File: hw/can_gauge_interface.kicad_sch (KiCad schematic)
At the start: 58 parts, among them J1 USB_B, J10 +5VA, J2 Conn_02x04_Top_Bottom, J3 Analog, J4 ICSP, J5 SPI Debug, J6 CAN ~{CS}, J7 ROM ~{CS}, J8 DAC ~{CS}, J9 Conn_01x04_Socket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

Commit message: routing
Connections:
- net DAC1_~{CS}: now also U1.12 (RB5/AN11/RX/DX)
- net DAC2_~{CS}: now also U1.10 (RB7/TX/CK)
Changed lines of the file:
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@@
+	(wire
+		(pts
+			(xy 298.45 80.01) (xy 308.61 80.01)
+		)
+		(stroke
+			(width 0)
+			(type default)
+		)
+	)
 	(wire
 		(pts
@@
 		(pts
 			(xy 233.68 152.4) (xy 233.68 182.88)
+		)
+		(stroke
+			(width 0)
+			(type default)
+		)
+	)
+	(wire
+		(pts
+			(xy 298.45 85.09) (xy 308.61 85.09)
 		)
 		(stroke
@@
 	)
 	(label "DAC1_~{CS}"
-		(at 318.77 46.99 0)
+		(at 298.45 80.01 0)
 		(effects
 			(font
@@
 	)
 	(label "DAC2_~{CS}"
-		(at 317.5 43.18 0)
-		(effects
-			(font
+		(at 298.45 85.09 0)
+		(effects
+			(font

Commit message: more routing
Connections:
- net DAC1_~{CS}: now also J8.2 (Pin_2), U1.10 (RB7/TX/CK); no longer J8.1 (Pin_1), U1.12 (RB5/AN11/RX/DX)
- net DAC2_~{CS}: now also J8.1 (Pin_1), U1.12 (RB5/AN11/RX/DX); no longer J8.2 (Pin_2), U1.10 (RB7/TX/CK)
- net Speed: now also U1.6 (CWG1B/C1OUT/C2OUT/RC4)
- net Tach: now also U1.7 (CLKR/C1IN3-/C2IN3-/DACOUT2/AN7/RC3)
- no-connect marks 7 -> 9
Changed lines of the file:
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@@
 	)
 	(no_connect
+		(at 410.21 67.31)
+	)
+	(no_connect
 		(at 200.66 185.42)
 	)
@@
 	)
 	(no_connect
+		(at 410.21 77.47)
+	)
+	(no_connect
 		(at 231.14 180.34)
 	)
@@
 	(wire
 		(pts
+			(xy 410.21 72.39) (xy 424.18 72.39)
+		)
+		(stroke
+			(width 0)
+			(type default)
+		)
+	)
+	(wire
+		(pts
 			(xy 391.16 134.62) (xy 391.16 139.7)
 		)
@@
 	(wire
 		(pts
+			(xy 410.21 69.85) (xy 424.18 69.85)
+		)
+		(stroke
+			(width 0)
+			(type default)
+		)
+	)
+	(wire
+		(pts
 			(xy 261.62 176.53) (xy 261.62 170.18)
 		)
@@
 	)
 	(label "DAC1_~{CS}"
-		(at 298.45 80.01 0)
+		(at 298.45 85.09 0)
 		(effects
 			(font
@@
 	)
 	(label "DAC2_~{CS}"
-		(at 298.45 85.09 0)
+		(at 298.45 80.01 0)
 		(effects
 			(font
@@
 	)
 	(label "DAC1_~{CS}"
-		(at 57.15 313.69 180)
+		(at 57.15 316.23 180)
 		(effects
 			(font
@@
 	)
 	(label "DAC2_~{CS}"
-		(at 57.15 316.23 180)
+		(at 57.15 313.69 180)
 		(effects
 			(font

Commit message: drc
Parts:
- J1: footprint Connector_USB:USB_B_Lumberg_2411_02_Horizontal -> footprints:USB_B_Lumberg_2411_02_Horizontal
- J2: footprint Connector_Molex:Molex_Mini-Fit_Jr_5569-08A2_2x04_P4.20mm_Horizontal -> footprints:Molex_Mini-Fit_Jr_5569-08A2_2x04_P4.20mm_Horizontal
- J3: footprint Connector_Molex:Molex_Mini-Fit_Jr_5569-06A2_2x03_P4.20mm_Horizontal -> footprints:Molex_Mini-Fit_Jr_5569-06A2_2x03_P4.20mm_Horizontal
- U5: footprint Package_SO:TI_SO-PowerPAD-8_ThermalVias -> Package_SO:TI_SO-PowerPAD-8
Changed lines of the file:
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@@
 			)
 		)
-		(property "Footprint" "Package_SO:TI_SO-PowerPAD-8_ThermalVias"
+		(property "Footprint" "Package_SO:TI_SO-PowerPAD-8"
 			(at 64.77 64.77 0)
 			(effects
@@
 			)
 		)
-		(property "Footprint" "Connector_Molex:Molex_Mini-Fit_Jr_5569-08A2_2x04_P4.20mm_Horizontal"
+		(property "Footprint" "footprints:Molex_Mini-Fit_Jr_5569-08A2_2x04_P4.20mm_Horizontal"
 			(at 49.53 233.68 0)
 			(effects
@@
 			)
 		)
-		(property "Footprint" "Connector_USB:USB_B_Lumberg_2411_02_Horizontal"
+		(property "Footprint" "footprints:USB_B_Lumberg_2411_02_Horizontal"
 			(at 44.45 205.74 0)
 			(effects
@@
 			)
 		)
-		(property "Footprint" "Connector_Molex:Molex_Mini-Fit_Jr_5569-06A2_2x03_P4.20mm_Horizontal"
+		(property "Footprint" "footprints:Molex_Mini-Fit_Jr_5569-06A2_2x03_P4.20mm_Horizontal"
 			(at 49.53 260.35 0)
 			(effects

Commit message: tune usb trace length
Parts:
- C10, C12, C13, C14, C15, C16, C17, J4, R10, R11, R6, R7, R9, U1, U2, U3, U4, U8, U9: now not fitted
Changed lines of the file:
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@@
 		(in_bom yes)
 		(on_board yes)
-		(dnp no)
+		(dnp yes)
 		(property "Reference" "C15"
 			(at 383.54 133.35 90)
@@
 		(in_bom yes)
 		(on_board yes)
-		(dnp no)
+		(dnp yes)
 		(property "Reference" "C14"
 			(at 266.7 143.51 90)
@@
 		(in_bom yes)
 		(on_board yes)
-		(dnp no)
+		(dnp yes)
 		(property "Reference" "U4"
 			(at 395.605 148.59 0)
@@
 		(in_bom yes)
 		(on_board yes)
-		(dnp no)
+		(dnp yes)
 		(property "Reference" "R7"
 			(at 200.025 152.4 0)
@@
 		(in_bom yes)
 		(on_board yes)
-		(dnp no)
+		(dnp yes)
 		(property "Reference" "R9"
 			(at 374.015 149.86 0)
@@
 		(in_bom yes)
 		(on_board yes)
-		(dnp no)
+		(dnp yes)
 		(property "Reference" "C13"
 			(at 201.93 135.89 90)
@@
 		(in_bom yes)
 		(on_board yes)
-		(dnp no)
+		(dnp yes)
 		(fields_autoplaced yes)
 		(property "Reference" "C12"
@@
 		(in_bom yes)
 		(on_board yes)
-		(dnp no)
+		(dnp yes)
 		(property "Reference" "C17"
 			(at 533.4 161.29 90)
@@
 		(in_bom yes)
 		(on_board yes)
-		(dnp no)
+		(dnp yes)
 		(property "Reference" "U8"
 			(at 528.955 111.76 0)
@@
 		(in_bom yes)
 		(on_board yes)
-		(dnp no)
+		(dnp yes)
 		(property "Reference" "U3"
 			(at 284.48 156.21 0)
@@
 		(in_bom yes)
 		(on_board yes)
-		(dnp no)
+		(dnp yes)
 		(property "Reference" "R6"
 			(at 274.955 58.42 0)
@@
 		(in_bom yes)
 		(on_board yes)
-		(dnp no)
+		(dnp yes)
 		(property "Reference" "C10"
 			(at 350.52 41.275 90)
@@
 		(in_bom yes)
 		(on_board yes)
-		(dnp no)
+		(dnp yes)
 		(property "Reference" "J4"
 			(at 36.195 168.275 0)
@@
 		(in_bom yes)
 		(on_board yes)
-		(dnp no)
+		(dnp yes)
 		(property "Reference" "U2"
 			(at 226.06 156.21 0)
@@
 		(in_bom yes)
 		(on_board yes)
-		(dnp no)
+		(dnp yes)
 		(property "Reference" "C16"
 			(at 533.4 97.79 90)
@@
 		(in_bom yes)
 		(on_board yes)
-		(dnp no)
+		(dnp yes)
 		(property "Reference" "U9"
 			(at 528.955 175.26 0)
@@
 		(in_bom yes)
 		(on_board yes)
-		(dnp no)
+		(dnp yes)
 		(property "Reference" "R10"
 			(at 502.285 111.76 0)
@@
 		(in_bom yes)
 		(on_board yes)
-		(dnp no)
+		(dnp yes)
 		(property "Reference" "U1"
 			(at 403.225 52.07 0)
@@
 		(in_bom yes)
 		(on_board yes)
-		(dnp no)
+		(dnp yes)
 		(property "Reference" "R11"
 			(at 502.285 175.26 0)

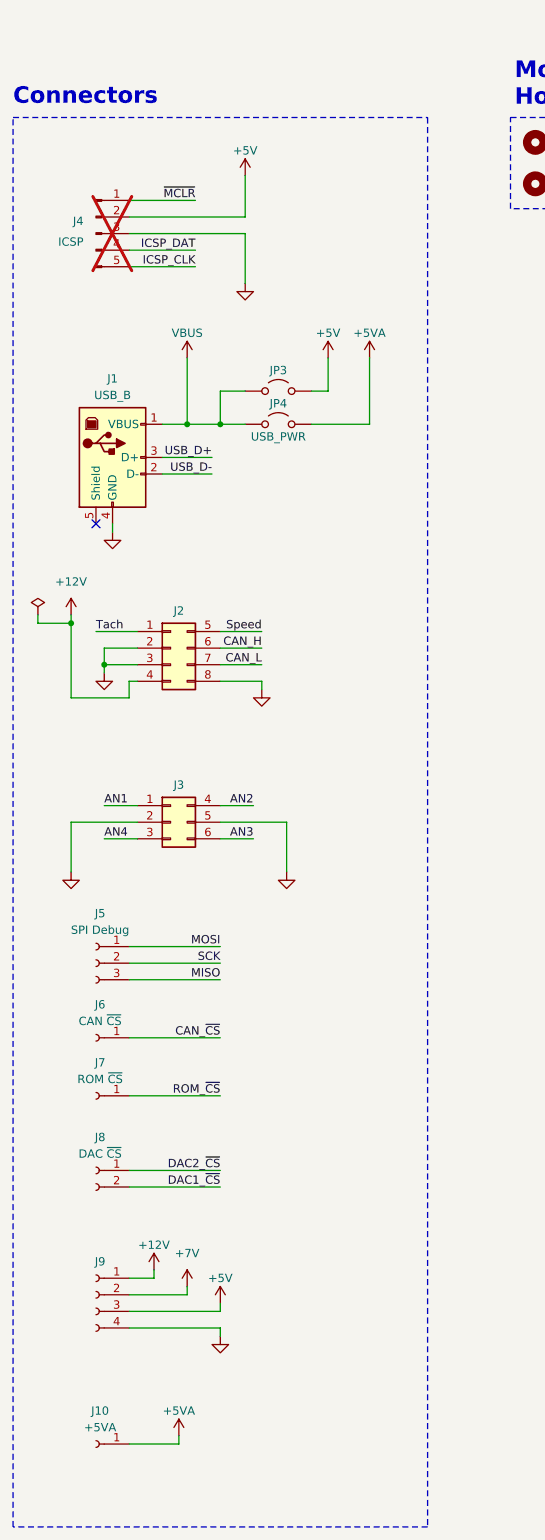
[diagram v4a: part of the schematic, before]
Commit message: removed usb vbus
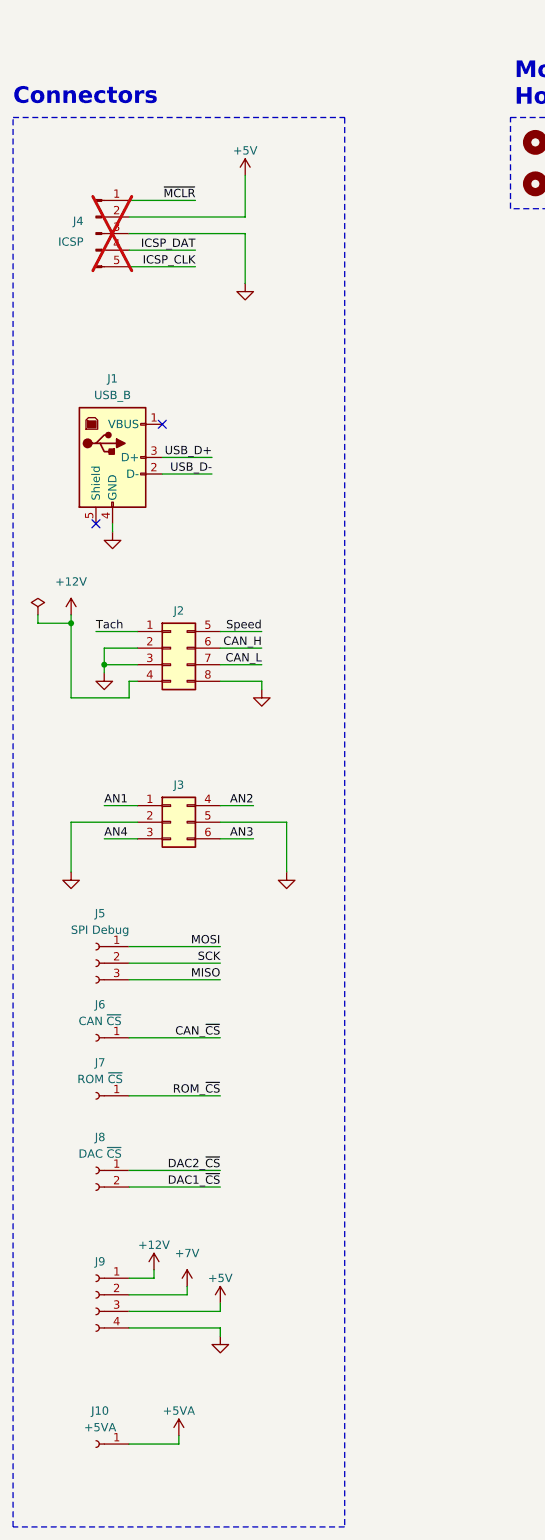
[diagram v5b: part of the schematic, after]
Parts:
- removed JP3, JP4: USB_PWR, Connector_PinSocket_2.54mm:PinSocket_1x02_P2.54mm_Vertical, symbol Jumper:Jumper_2_Open
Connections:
- net VBUS: no longer names the net of J1.1 (VBUS)
- no-connect marks 9 -> 10

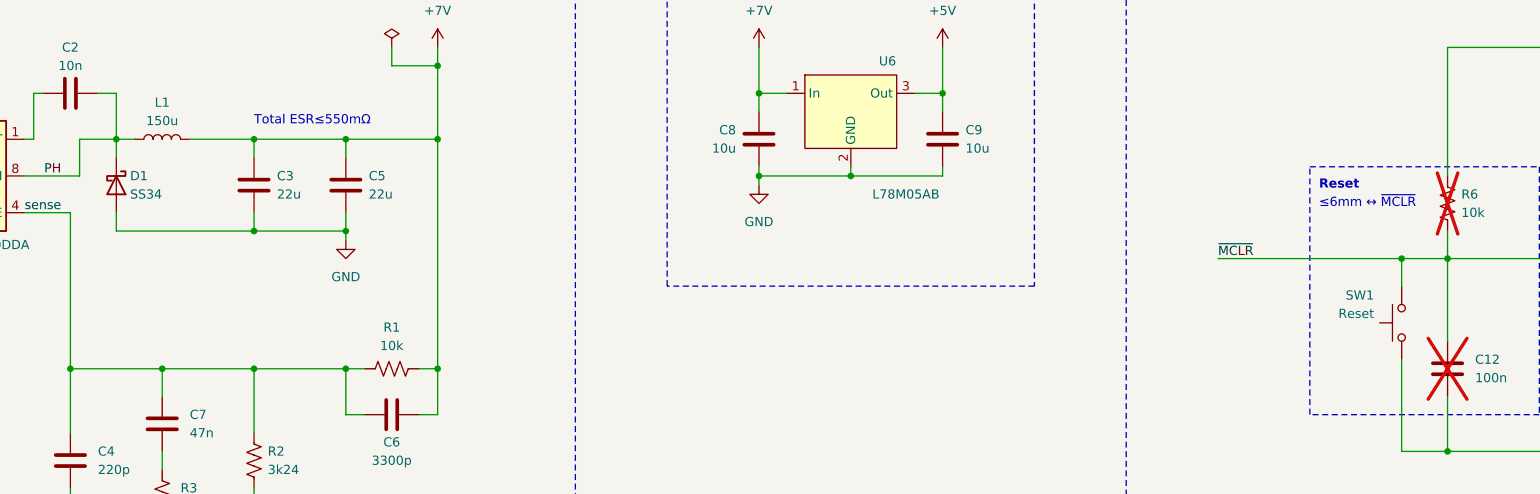
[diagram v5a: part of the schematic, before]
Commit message: gnd pours
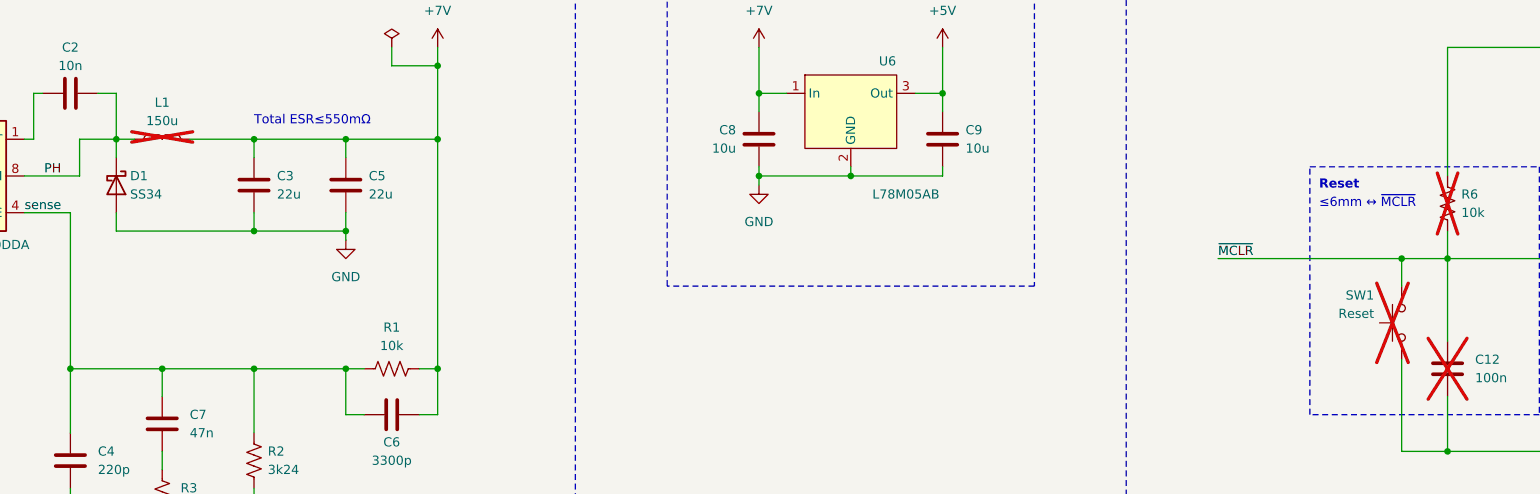
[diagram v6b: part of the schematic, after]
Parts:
- JP2: now in the parts list
- L1: footprint Inductor_SMD:L_12x12mm_H8mm -> Inductor_SMD:L_Wuerth_WE-PD-Typ-LS_Handsoldering; now not fitted
- SW1: now not fitted
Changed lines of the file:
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@@
 	(title_block
 		(title "CAN Gauge Interface")
-		(date "2025-09-19")
-		(rev "0.1")
+		(date "2025-10-01")
+		(rev "0.2")
 		(company "Sam Anthony")
 	)
@@
 		(unit 1)
 		(exclude_from_sim no)
-		(in_bom no)
+		(in_bom yes)
 		(on_board yes)
 		(dnp no)
@@
 		(in_bom yes)
 		(on_board yes)
-		(dnp no)
+		(dnp yes)
 		(fields_autoplaced yes)
 		(property "Reference" "L1"
@@
 			)
 		)
-		(property "Footprint" "Inductor_SMD:L_12x12mm_H8mm"
+		(property "Footprint" "Inductor_SMD:L_Wuerth_WE-PD-Typ-LS_Handsoldering"
 			(at 95.25 50.8 0)
 			(effects
@@
 			)
 		)
-		(property "Datasheet" "~"
+		(property "Datasheet" "https://www.we-online.com/components/products/datasheet/7447706151.pdf"
 			(at 95.25 50.8 0)
 			(effects
@@
 		(in_bom yes)
 		(on_board yes)
-		(dnp no)
+		(dnp yes)
 		(property "Reference" "SW1"
 			(at 262.89 72.39 90)

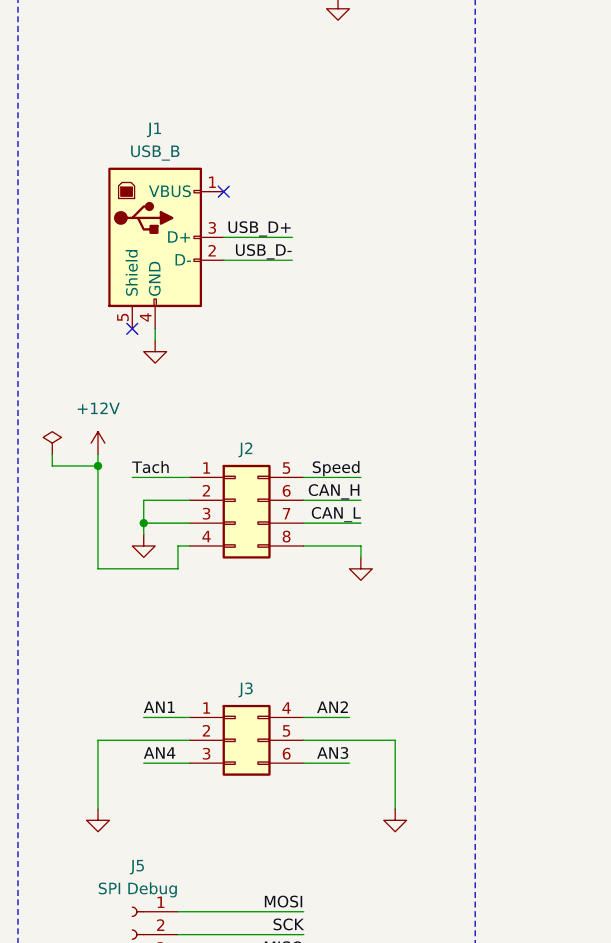
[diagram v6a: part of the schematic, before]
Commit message: connector 3d models
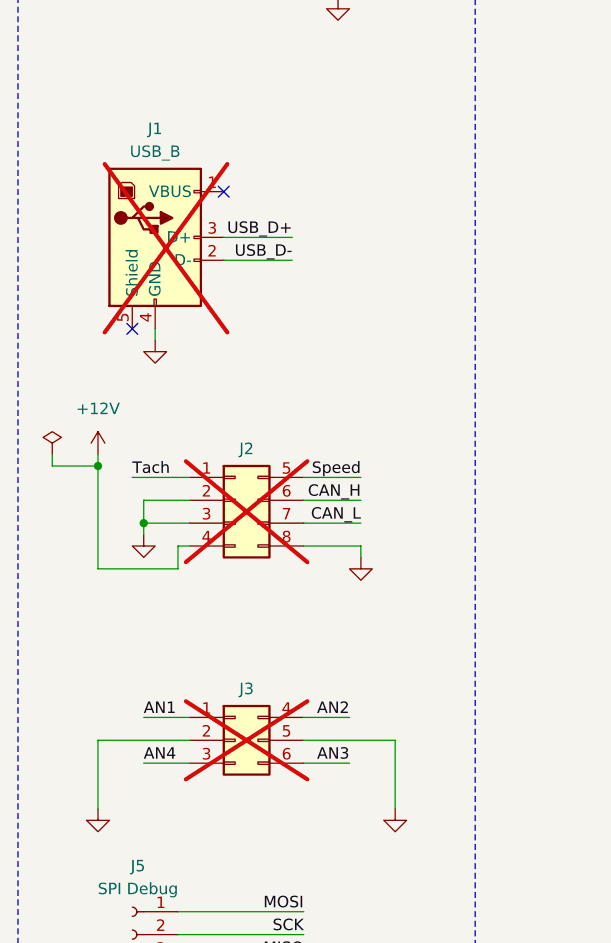
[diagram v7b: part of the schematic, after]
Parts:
- J1: footprint footprints:USB_B_Lumberg_2411_02_Horizontal -> USB_B_Samtec_USB-B-S-F-W-TH:SAMTEC_USB-B-S-X-X-TH; now not fitted
- J2, J3: now not fitted
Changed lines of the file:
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@@
 	)
 	(no_connect
-		(at 38.1 214.63)
-	)
-	(no_connect
 		(at 48.26 199.39)
 	)
@@
 		(at 231.14 180.34)
 	)
+	(no_connect
+		(at 38.1 214.63)
+	)
 	(wire
 		(pts
@@
 		(in_bom yes)
 		(on_board yes)
-		(dnp no)
+		(dnp yes)
 		(property "Reference" "J2"
 			(at 50.8 227.965 0)
@@
 		(in_bom yes)
 		(on_board yes)
-		(dnp no)
+		(dnp yes)
 		(property "Reference" "J1"
 			(at 40.64 192.405 0)
@@
 			)
 		)
-		(property "Footprint" "footprints:USB_B_Lumberg_2411_02_Horizontal"
+		(property "Footprint" "USB_B_Samtec_USB-B-S-F-W-TH:SAMTEC_USB-B-S-X-X-TH"
 			(at 44.45 205.74 0)
 			(effects
@@
 			)
 		)
-		(property "Datasheet" "~"
+		(property "Datasheet" "https://suddendocs.samtec.com/prints/usb-b-s-x-x-th-x-xx-mkt.pdf"
 			(at 44.45 205.74 0)
 			(effects
@@
 		(in_bom yes)
 		(on_board yes)
-		(dnp no)
+		(dnp yes)
 		(property "Reference" "J3"
 			(at 50.8 254.635 0)

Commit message: manufacturing
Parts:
- H1, H2, H3, H4, J10, J5, J6, J7, J8, J9: now not fitted
- JP1: renamed from JP2; now not fitted
- JP2: renamed from JP5; now not fitted
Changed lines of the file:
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@@
 		(in_bom yes)
 		(on_board yes)
-		(dnp no)
-		(property "Reference" "JP2"
+		(dnp yes)
+		(property "Reference" "JP1"
 			(at 433.705 66.04 90)
 			(effects
@@
 			(project ""
 				(path "/11aaed46-be21-4424-b899-cb4c1a8c3e5f"
-					(reference "JP2")
+					(reference "JP1")
 					(unit 1)
 				)
@@
 		(in_bom no)
 		(on_board yes)
-		(dnp no)
+		(dnp yes)
 		(fields_autoplaced yes)
 		(property "Reference" "H1"
@@
 		(in_bom yes)
 		(on_board yes)
-		(dnp no)
+		(dnp yes)
 		(fields_autoplaced yes)
 		(property "Reference" "J9"
@@
 		(in_bom yes)
 		(on_board yes)
-		(dnp no)
+		(dnp yes)
 		(fields_autoplaced yes)
 		(property "Reference" "J6"
@@
 		(in_bom yes)
 		(on_board yes)
-		(dnp no)
+		(dnp yes)
 		(property "Reference" "J10"
 			(at 38.735 350.52 0)
@@
 		(in_bom yes)
 		(on_board yes)
-		(dnp no)
+		(dnp yes)
 		(fields_autoplaced yes)
 		(property "Reference" "J5"
@@
 		(in_bom no)
 		(on_board yes)
-		(dnp no)
+		(dnp yes)
 		(fields_autoplaced yes)
 		(property "Reference" "H4"
@@
 		(in_bom no)
 		(on_board yes)
-		(dnp no)
+		(dnp yes)
 		(fields_autoplaced yes)
 		(property "Reference" "H2"
@@
 		(in_bom yes)
 		(on_board yes)
-		(dnp no)
-		(property "Reference" "JP5"
+		(dnp yes)
+		(property "Reference" "JP2"
 			(at 299.72 151.765 0)
 			(effects
@@
 			(project ""
 				(path "/11aaed46-be21-4424-b899-cb4c1a8c3e5f"
-					(reference "JP5")
+					(reference "JP2")
 					(unit 1)
 				)
@@
 		(in_bom no)
 		(on_board yes)
-		(dnp no)
+		(dnp yes)
 		(fields_autoplaced yes)
 		(property "Reference" "H3"
@@
 		(in_bom yes)
 		(on_board yes)
-		(dnp no)
+		(dnp yes)
 		(fields_autoplaced yes)
 		(property "Reference" "J8"
@@
 		(in_bom yes)
 		(on_board yes)
-		(dnp no)
+		(dnp yes)
 		(fields_autoplaced yes)
 		(property "Reference" "J7"
